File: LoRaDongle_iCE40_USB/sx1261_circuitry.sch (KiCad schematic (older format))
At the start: 38 parts

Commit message: changed to sx1261
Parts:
- removed C?: 100nF, Capacitor_SMD:C_0402_1005Metric, symbol Device:C
- removed C?: 10pF, Capacitor_SMD:C_0402_1005Metric, symbol Device:C
- removed FB?: 10R/100MHz, Inductor_SMD:L_0402_1005Metric, symbol Device:Ferrite_Bead_Small
- removed R?: 220R, Resistor_SMD:R_0402_1005Metric, symbol Device:R
- removed U?: 4259-63, digikey-footprints:SOT-363, symbol dk_RF-Switches:4259-63
- removed Y?: TYETBCSANF-32.000000, TY, symbol TYETBCSANF-32.000000:TYETBCSANF-32.000000
- added C? (x3): 470pF, Capacitor_SMD:C_0402_1005Metric, symbol Device:C
- added J?: RF_Shield_One_Piece, symbol Device:RF_Shield_One_Piece
- added U?: SKY13587-378LF, SW_SKYA21012:SW_SKYA21012, symbol LoRaDongle:SKY13587-378LF
- added Y?: Crystal, Crystal:Crystal_SMD_2016-4Pin_2.0x1.6mm, symbol Device:Crystal
- C? (x2): value 1nF -> 33pF; Part Number GRM155R72A102KA01D -> CGA2B2C0G1H330J050BA
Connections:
- net labels added: VCTL1, VCTL2
- wire segments 115 -> 114
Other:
- note added: "To be completed"
- moved on the sheet: C?, J?, L?, R?

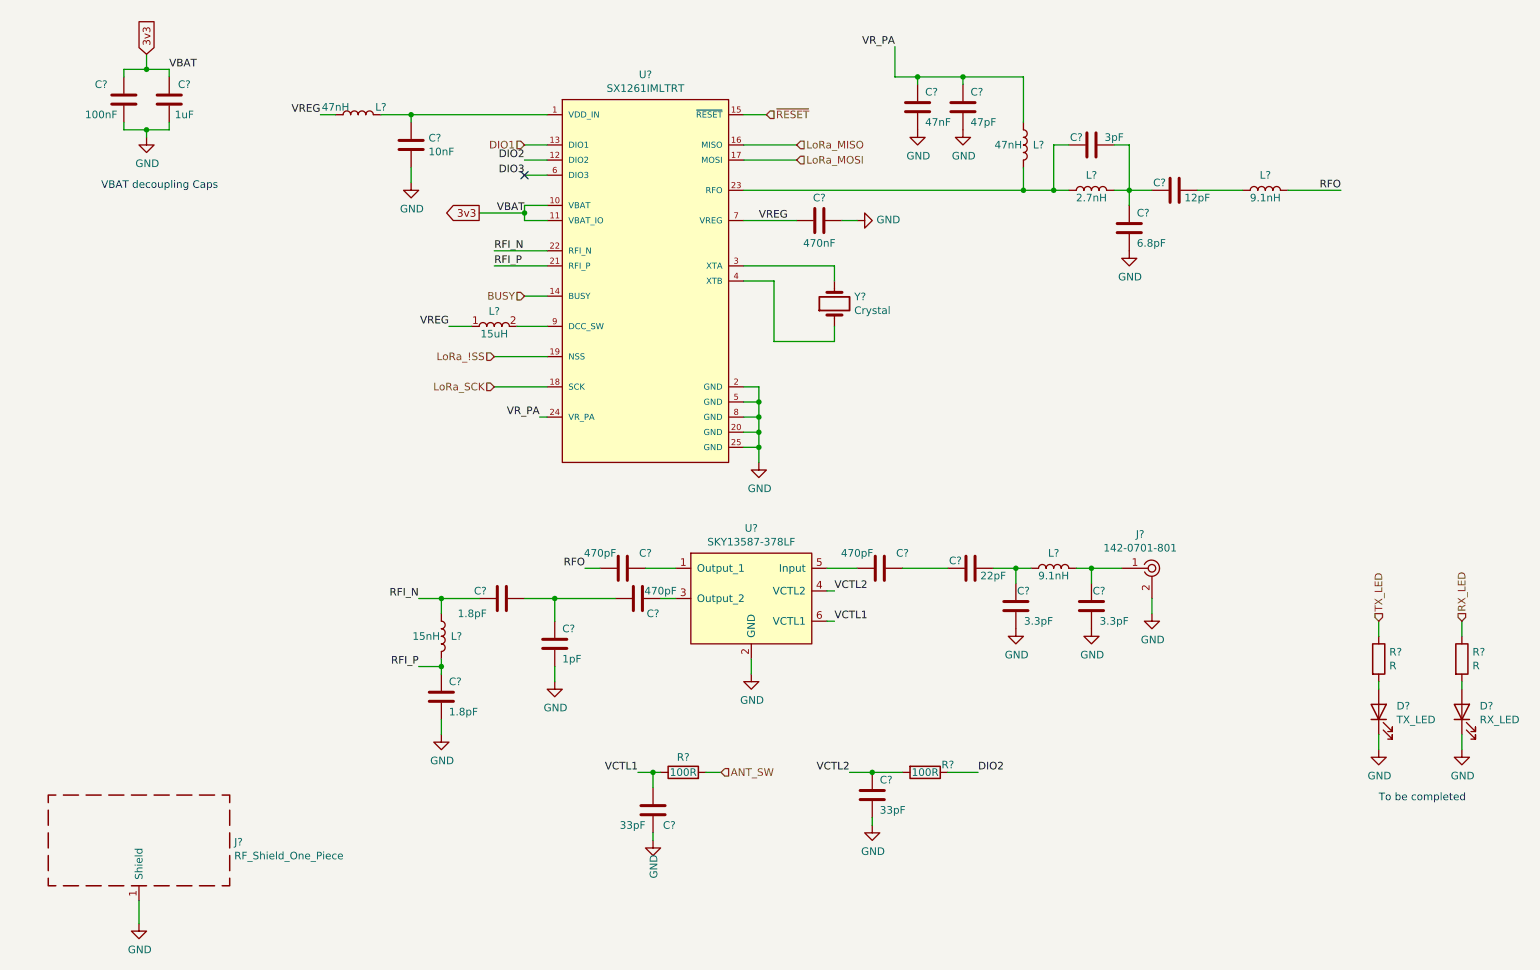
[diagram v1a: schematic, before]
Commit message: added footprints
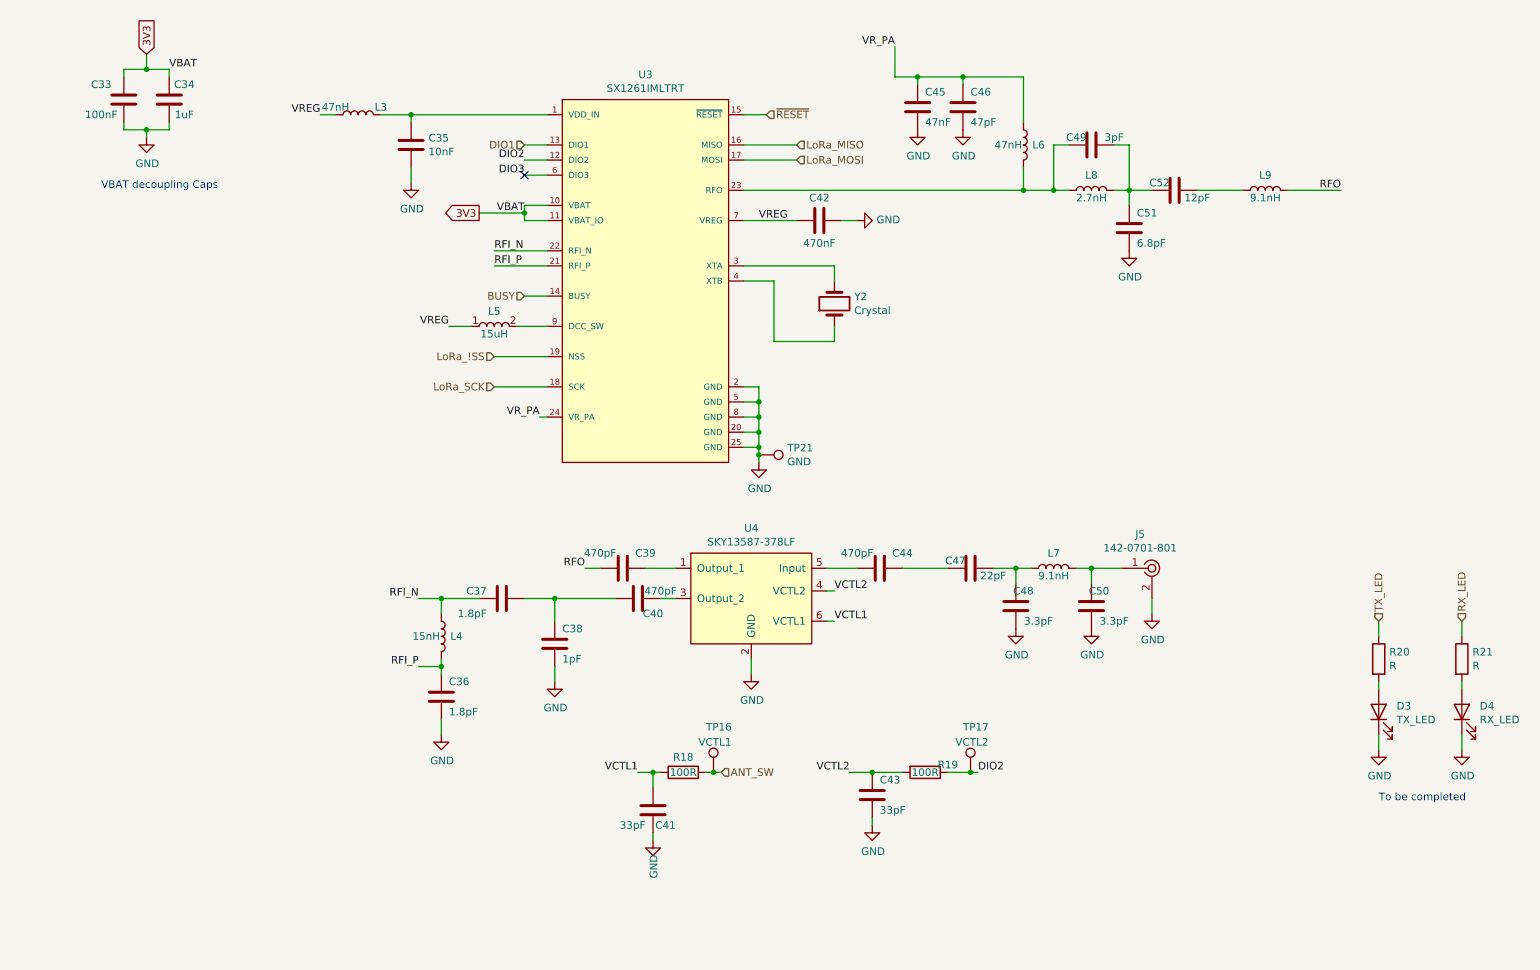
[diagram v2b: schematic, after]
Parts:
- removed J?: RF_Shield_One_Piece, symbol Device:RF_Shield_One_Piece
- added TP16: VCTL1, TestPoint:TestPoint_Pad_2.0x2.0mm, symbol Connector:TestPoint
- added TP17: VCTL2, TestPoint:TestPoint_Pad_2.0x2.0mm, symbol Connector:TestPoint
- added TP21: GND, TestPoint:TestPoint_Pad_D2.5mm, symbol Connector:TestPoint
- D3, D4: renamed from D?; footprint (none) -> LED_SMD:LED_0603_1608Metric
- L5: renamed from L?; footprint VLS2016 -> KiCad_VLS201610CX-150M-1:VLS2016
- R20, R21: renamed from R?; footprint (none) -> Resistor_SMD:R_0402_1005Metric
- U3: renamed from U?; footprint Semtech-QFN24-0-0-* -> sx1261-footprint:Semtech-QFN24-0-0-0
- gave numbers to parts that had none: 31
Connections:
- net ANT_SW: now also TP16.1
- net DIO2: now also TP17.1
- net GND: now also TP21.1
- net 3v3 renamed 3V3

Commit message: PCB Layout V01
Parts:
- added J8: Jumper, Connector_PinHeader_2.54mm:PinHeader_1x02_P2.54mm_Vertical, symbol Device:Jumper
- C33, C34, C35, C36, C37, C38, C39, C40, C41, C42, C43, C44, C45, C46, C47, C48, C49, C50, C51, C52: footprint Capacitor_SMD:C_0402_1005Metric -> Capacitor_SMD:C_0402_1005Metric_Pad0.74x0.62mm_HandSolder
- D3: value TX_LED -> TX; footprint LED_SMD:LED_0603_1608Metric -> LED_SMD:LED_0603_1608Metric_Pad1.05x0.95mm_HandSolder
- D4: value RX_LED -> RX; footprint LED_SMD:LED_0603_1608Metric -> LED_SMD:LED_0603_1608Metric_Pad1.05x0.95mm_HandSolder
- GND1: renamed from TP21; footprint TestPoint:TestPoint_Pad_D2.5mm -> TestPoint:TestPoint_Pad_D1.0mm
- L3, L4, L6, L7, L8, L9: footprint Inductor_SMD:L_0402_1005Metric -> Inductor_SMD:L_0402_1005Metric_Pad0.77x0.64mm_HandSolder
- R18, R19, R20, R21: footprint Resistor_SMD:R_0402_1005Metric -> Resistor_SMD:R_0402_1005Metric_Pad0.72x0.64mm_HandSolder
- VCTL1: renamed from TP16; footprint TestPoint:TestPoint_Pad_2.0x2.0mm -> TestPoint:TestPoint_Pad_D1.0mm
- VCTL2: renamed from TP17; footprint TestPoint:TestPoint_Pad_2.0x2.0mm -> TestPoint:TestPoint_Pad_D1.0mm
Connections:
- net 3V3: now also J8.1; no longer C33.2, C34.2, U3.10 (VBAT), U3.11 (VBAT_IO)
- new net RadioPower: C33.2, C34.2, J8.2, U3.10 (VBAT), U3.11 (VBAT_IO)
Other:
- moved on the sheet: C33, C34

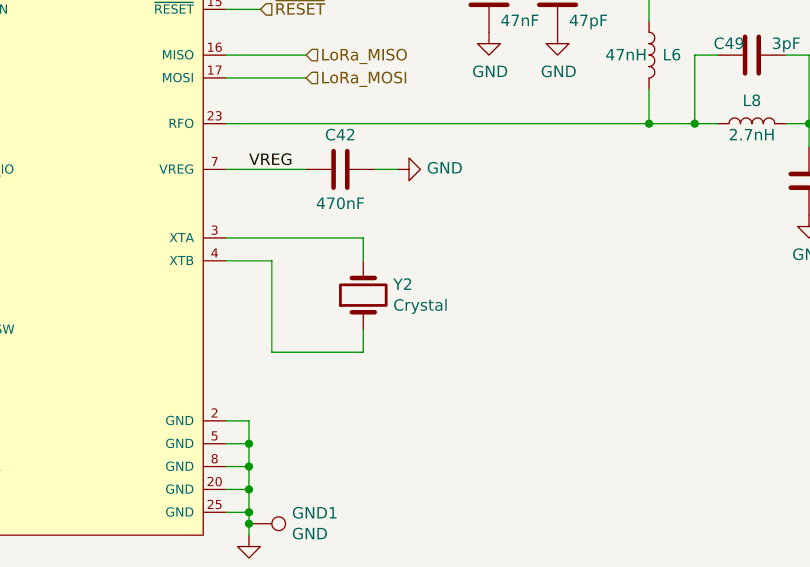
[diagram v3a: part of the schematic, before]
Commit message: added more traces
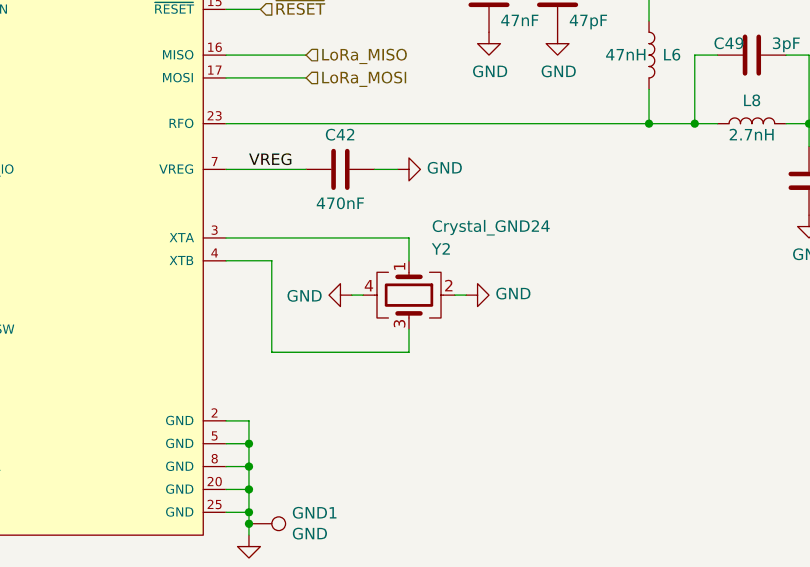
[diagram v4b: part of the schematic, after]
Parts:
- removed Y2: Crystal, Crystal:Crystal_SMD_2016-4Pin_2.0x1.6mm, symbol Device:Crystal
- added Y2: Crystal_GND24, Crystal:Crystal_SMD_2520-4Pin_2.5x2.0mm, symbol Device:Crystal_GND24
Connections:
- net GND: now also Y2.2, Y2.4
- net at U3.4 (XTB): now also Y2.3
- net at U3.3 (XTA): now also Y2.1
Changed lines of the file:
@@
-	0    -1   -1   0
-$EndComp
-$Comp
-L Device:Crystal Y2
-U 1 1 61B3BC34
-P 6150 2650
-F 0 "Y2" V 6196 2519 50  0000 R CNN
-F 1 "Crystal" V 6105 2519 50  0000 R CNN
-F 2 "Crystal:Crystal_SMD_2016-4Pin_2.0x1.6mm" H 6150 2650 50  0001 C CNN
-F 3 "~" H 6150 2650 50  0001 C CNN
-F 4 "XRCGB32M000F2P00R0" V 6150 2650 50  0001 C CNN "Part Number"
-	1    6150 2650
 	0    -1   -1   0
 $EndComp
 Wire Wire Line
 	5550 2500 5750 2500
-Wire Wire Line
-	6150 2500 6150 2400
-Wire Wire Line
-	5550 2400 6150 2400
-Wire Wire Line
-	6150 2800 6150 2900
-Wire Wire Line
-	6150 2900 5750 2900
 Wire Wire Line
 	5750 2500 5750 2900
@@
 	0    1    1    0
 $EndComp
+$Comp
+L Device:Crystal_GND24 Y2
+U 1 1 61D1DB8F
+P 6350 2650
+F 0 "Y2" V 6150 2750 50  0000 L CNN
+F 1 "Crystal_GND24" V 6050 2750 50  0000 L CNN
+F 2 "Crystal:Crystal_SMD_2520-4Pin_2.5x2.0mm" H 6350 2650 50  0001 C CNN
+F 3 "~" H 6350 2650 50  0001 C CNN
+F 4 "ECS-320-10-36B-CKM-TR" H 6350 2650 50  0001 C CNN "Part Number"
+	1    6350 2650
+	0    1    1    0
+$EndComp
+Wire Wire Line
+	6150 2650 6100 2650
+Wire Wire Line
+	6350 2800 6350 2900
+Wire Wire Line
+	5750 2900 6350 2900
+Wire Wire Line
+	6350 2500 6350 2400
+Wire Wire Line
+	5550 2400 6350 2400
+$Comp
+L power:GND #PWR?
+U 1 1 61D5CDCE
+P 6100 2650
+F 0 "#PWR?" H 6100 2400 50  0001 C CNN
+F 1 "GND" V 6105 2522 50  0000 R CNN
+F 2 "" H 6100 2650 50  0001 C CNN
+F 3 "" H 6100 2650 50  0001 C CNN
+	1    6100 2650
+	0    1    1    0
+$EndComp
+$Comp
+L power:GND #PWR?
+U 1 1 61D5D432
+P 6600 2650
+F 0 "#PWR?" H 6600 2400 50  0001 C CNN
+F 1 "GND" V 6605 2522 50  0000 R CNN
+F 2 "" H 6600 2650 50  0001 C CNN
+F 3 "" H 6600 2650 50  0001 C CNN
+	1    6600 2650
+	0    -1   -1   0
+$EndComp
+Wire Wire Line
+	6550 2650 6600 2650
 $EndSCHEMATC

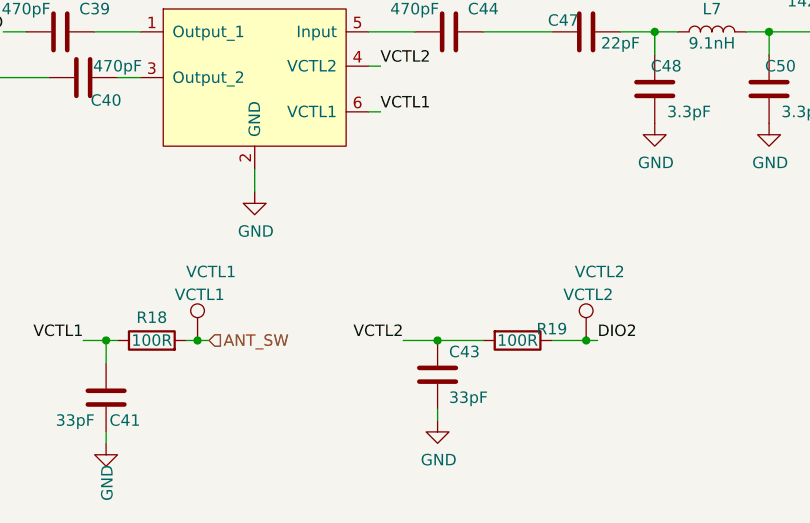
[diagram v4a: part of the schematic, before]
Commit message: breakout of bga part
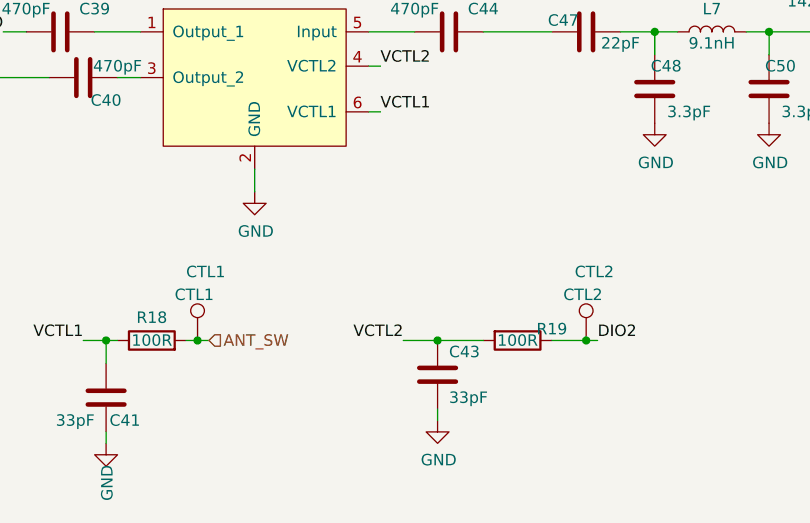
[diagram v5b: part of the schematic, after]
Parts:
- CTL1: renamed from VCTL1; value VCTL1 -> CTL1
- CTL2: renamed from VCTL2; value VCTL2 -> CTL2
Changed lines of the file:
@@
 	6900 5750 7050 5750
 $Comp
-L Connector:TestPoint VCTL2
+L Connector:TestPoint CTL2
 U 1 1 61D45A7D
 P 7050 5750
-F 0 "VCTL2" H 7000 6050 50  0000 L CNN
-F 1 "VCTL2" H 6950 5950 50  0000 L CNN
+F 0 "CTL2" H 7000 6050 50  0000 L CNN
+F 1 "CTL2" H 6950 5950 50  0000 L CNN
 F 2 "TestPoint:TestPoint_Pad_D1.0mm" H 7250 5750 50  0001 C CNN
 F 3 "~" H 7250 5750 50  0001 C CNN
@@
 Connection ~ 5350 5750
 $Comp
-L Connector:TestPoint VCTL1
+L Connector:TestPoint CTL1
 U 1 1 61D47C1E
 P 5350 5750
-F 0 "VCTL1" H 5300 6050 50  0000 L CNN
-F 1 "VCTL1" H 5250 5950 50  0000 L CNN
+F 0 "CTL1" H 5300 6050 50  0000 L CNN
+F 1 "CTL1" H 5250 5950 50  0000 L CNN
 F 2 "TestPoint:TestPoint_Pad_D1.0mm" H 5550 5750 50  0001 C CNN
 F 3 "~" H 5550 5750 50  0001 C CNN
@@
 	5550 2400 6350 2400
 $Comp
-L power:GND #PWR?
+L power:GND #PWR0101
 U 1 1 61D5CDCE
 P 6100 2650
-F 0 "#PWR?" H 6100 2400 50  0001 C CNN
+F 0 "#PWR0101" H 6100 2400 50  0001 C CNN
 F 1 "GND" V 6105 2522 50  0000 R CNN
 F 2 "" H 6100 2650 50  0001 C CNN
@@
 $EndComp
 $Comp
-L power:GND #PWR?
+L power:GND #PWR0112
 U 1 1 61D5D432
 P 6600 2650
-F 0 "#PWR?" H 6600 2400 50  0001 C CNN
+F 0 "#PWR0112" H 6600 2400 50  0001 C CNN
 F 1 "GND" V 6605 2522 50  0000 R CNN
 F 2 "" H 6600 2650 50  0001 C CNN
